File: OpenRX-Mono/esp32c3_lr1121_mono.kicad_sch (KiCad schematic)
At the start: 45 parts, among them T1 0900PC16J0042001E, U1 ESP32-C3FH4, U2 TLV75533PDQNR, U3 RFX2401C, U4 LR1121IMLTRT, U5 OW2EL89CENUXFMYLC-32M, X1 CJ17-400001010B20

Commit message: Add LCSC C430052 for 24nH XTAL_P inductor on Mono
Mono L2 (24nH 0201) was missing LCSC field.
Lite still needs 24nH inductor added in KiCad GUI.
Gemini is parked — still a Mono copy, not yet dual-radio.
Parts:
- added L2: 24nH, Inductor_SMD:L_0201_0603Metric, symbol Device:L
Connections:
- net XTAL_P: now also L2.2; no longer C6.1, X1.1
- new net: C6.1, L2.1, X1.1
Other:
- moved on the sheet: AE1, C1, C10, C11, C12, C13, C19, C2, C20, C21, C22, C23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

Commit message: OpenRX-Gemini: dual LR1121 schematic complete, 0 ERC errors
- Radio 1 (U4): sub-GHz via Johanson IPD → JP1 UFL
- Radio 2 (U9): 2.4GHz via RFX2401C (U10) → DEA (USB2) → JP3 UFL
- Shared SPI bus (SCK/MISO/MOSI), separate NSS/IRQ/BUSY/RST per radio
- Radio 2 control: GPIO10=NSS2, GPIO9=IRQ2, GPIO1=BUSY2, GPIO0=RST2
- FEM driven by Radio 2 RFSW (DIO5→RXEN, DIO6→TXEN)
- Radio 1 DIO5/DIO6 have 100k pull-downs (disconnected from FEM)
- No LED (GPIO10 used for NSS2), no boot button (GPIO9 used for IRQ2)
- Still needs: 10k pull-up on NSS2
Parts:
- L2: LCSC C430052 -> C206441
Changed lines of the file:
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@@
 			)
 		)
-		(property "LCSC" ""
+		(property "LCSC" "C206441"
 			(at -246.38 2.54 0)
 			(hide yes)
@@
 			(effects
 				(font
-					(size 1.27 1.27)
-				)
-			)
-		)
-		(property "LCSC" "C430052"
-			(at 0 0 0)
-			(show_name no)
-			(do_not_autoplace no)
-			(hide yes)
-			(effects
-				(font

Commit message: Swap all solder pads to 1.2x2.0mm rounded (25%) across Lite, Mono, Gemini
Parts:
- TP1, TP2, TP3, TP4: footprint OpenRX-Shared:SolderPad_1.0x1.5mm -> OpenRX-Shared:SolderPad_1.2x2.0mm
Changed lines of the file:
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@@
 			)
 		)
-		(property "Footprint" "OpenRX-Shared:SolderPad_1.0x1.5mm"
+		(property "Footprint" "OpenRX-Shared:SolderPad_1.2x2.0mm"
 			(at 152.4 116.84 0)
 			(hide yes)
@@
 			)
 		)
-		(property "Footprint" "OpenRX-Shared:SolderPad_1.0x1.5mm"
+		(property "Footprint" "OpenRX-Shared:SolderPad_1.2x2.0mm"
 			(at 82.55 72.39 0)
 			(hide yes)
@@
 			)
 		)
-		(property "Footprint" "OpenRX-Shared:SolderPad_1.0x1.5mm"
+		(property "Footprint" "OpenRX-Shared:SolderPad_1.2x2.0mm"
 			(at 82.55 74.93 0)
 			(hide yes)
@@
 			)
 		)
-		(property "Footprint" "OpenRX-Shared:SolderPad_1.0x1.5mm"
+		(property "Footprint" "OpenRX-Shared:SolderPad_1.2x2.0mm"
 			(at 152.4 106.68 0)
 			(hide yes)

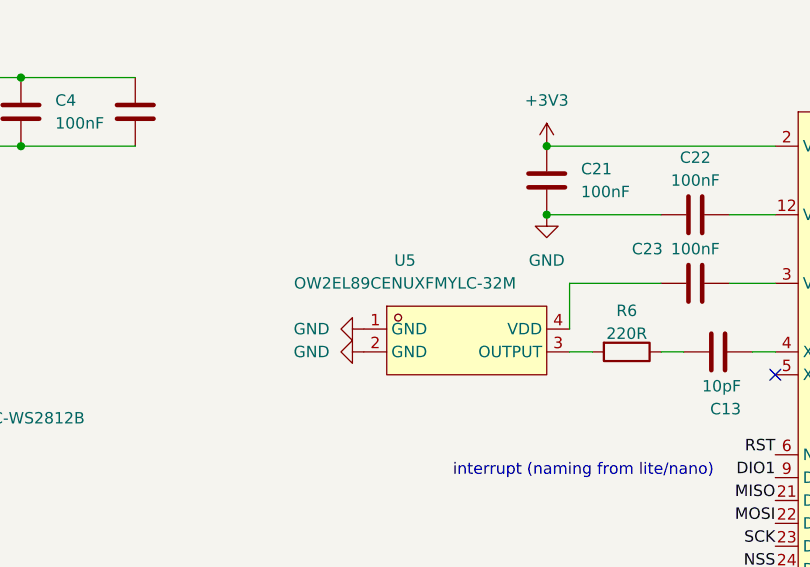
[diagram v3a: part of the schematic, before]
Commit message: Swap 32MHz TCXO to smaller 2016 package (C22381772)
OW2EL89 (3225, 3.2x2.5mm) → OW7EL89 (2016, 2.0x1.6mm)
Same YXC family, same pinout, same specs. Saves 1.2x0.9mm per TCXO.
Affects Mono (1x) and Gemini (2x).
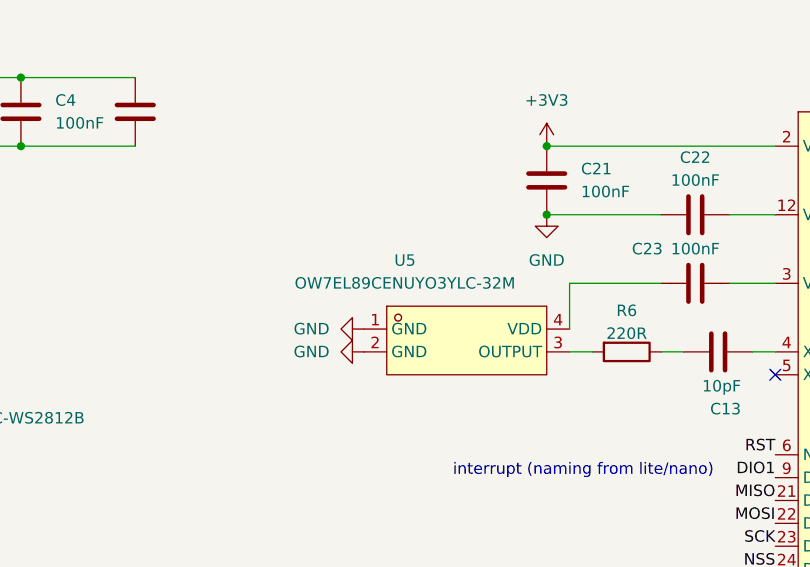
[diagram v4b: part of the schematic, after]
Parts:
- U5: value OW2EL89CENUXFMYLC-32M -> OW7EL89CENUYO3YLC-32M; footprint OpenRX-Shared:OSC-SMD_4P-L3.2-W2.5-BL -> OpenRX-Shared:OSC-SMD_4P-L2.0-W1.6-BL_TXC_7Z; symbol OpenRX-Shared:OW2EL89CENUXFMYLC-32M -> OpenRX-Shared:OW7EL89CENUYO3YLC-32M; LCSC C22434888 -> C22381772; LCSC Part C22434888 -> C22381772
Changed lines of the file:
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@@
 	)
 	(symbol
-		(lib_id "OpenRX-Shared:OW2EL89CENUXFMYLC-32M")
+		(lib_id "OpenRX-Shared:OW7EL89CENUYO3YLC-32M")
 		(at 217.17 58.42 0)
 		(unit 1)
@@
 			)
 		)
-		(property "Value" "OW2EL89CENUXFMYLC-32M"
+		(property "Value" "OW7EL89CENUYO3YLC-32M"
 			(at 210.312 52.07 0)
 			(show_name no)
@@
 			)
 		)
-		(property "Footprint" "OpenRX-Shared:OSC-SMD_4P-L3.2-W2.5-BL"
+		(property "Footprint" "OpenRX-Shared:OSC-SMD_4P-L2.0-W1.6-BL_TXC_7Z"
 			(at 217.17 67.31 0)
 			(hide yes)
@@
 			)
 		)
-		(property "LCSC Part" "C22434888"
+		(property "LCSC Part" "C22381772"
 			(at 217.17 69.85 0)
 			(hide yes)
@@
 			)
 		)
-		(property "LCSC" "C22434888"
+		(property "LCSC" "C22381772"
 			(at -15.24 0 0)
 			(hide yes)

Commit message: FINAL_NETLIST v3: SKY13588 as band combiner, RFX2401C kept for 100mW
Based on RadioMaster XR4 teardown analysis:
- SKY13588 serves as both sub-GHz path switch AND band combiner
- Johanson IPD in direct-tie mode (RX/TX_LP/TX_HP joined) → SKY13588 J1
- 2.4GHz: RFIO_HF → DEA LPF → RFX2401C → SKY13588 J2
- SKY13588 RFC → DC block → UFL → dual-band antenna
- RFX2401C kept for 100mW market parity
- Button imported (C2976675, 3x2mm SMD)
- RFSW truth table: DIO7/DIO8 control band, DIO5/DIO6 control RFX2401C
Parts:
- removed C26: 1uF, Capacitor_SMD:C_0201_0603Metric, symbol Device:C
- removed JP2: U.FL-R-SMT-1(80), OpenRX-Shared:RF-SMD_FRF05002-JSS103M, symbol OpenRX-Shared:U.FL-R-SMT-1(80)
- removed U3: RFX2401C, OpenRX-Shared:QFN-16_L3.0-W3.0-P0.50-BL-EP1.7, symbol OpenRX-Shared:RFX2401C
- removed USB1: DEA102700LT-6307A2, OpenRX-Shared:FILTER-SMD_4P-L1.0-W0.5-L_DEA102700LT-XXX, symbol OpenRX-Shared:DEA102700LT-6307A2
- added U3: TS2306A 240GF MSM 9_C2976675, OpenRX-Shared:SW-SMD_4P-L3.0-W2.0-P0.85-LS3.5, symbol OpenRX-Shared:TS2306A240GFMSM9_C2976675
- added U6: SKY13588-460LF, OpenRX-Shared:QFN-12_L2.0-W2.0-P0.50-BL-EP0.8, symbol OpenRX-Shared:SKY13588-460LF
- added USB2: DEA102700LT-6307A2, OpenRX-Shared:FILTER-SMD_4P-L1.0-W0.5-L_DEA102700LT-XXX, symbol OpenRX-Shared:DEA102700LT-6307A2
- C25: value 220pF -> 100nF; LCSC C62548 -> C76939
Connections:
- net RXEN is gone; now on an unnamed net: U4.20 (DIO5)
- net TXEN is gone; now on an unnamed net: U4.19 (DIO6)
- net +3V3: now also U6.6 (VDD)
- net GND: now also C23.1, U3.2, U6.10 (GND), U6.12 (GND), U6.13 (EP), U6.2 (GND), U6.7 (GND), U6.8 (GND), USB2.2 (GND), USB2.4 (GND)
- net LED: now also U1.14 (GPIO8); no longer U1.16 (GPIO10)
- net MISO: now also U1.10 (MTDI); no longer U1.12 (MTCK)
- net MOSI: now also U1.9 (MTMS); no longer U1.13 (MTDO)
- net SCK: now also U1.12 (MTCK); no longer U1.9 (MTMS)
- net IRQ1: now reaches U1.5 (XTAL_32K_N)
- net IRQ1: now also U4.9 (DIO9)
- net at U5.4 (VDD): now also C23.2, U4.3 (VTCXO); no longer C23.1
- net at R5.2: no longer U4.10 (DIO8)
- net at R7.2: no longer U4.11 (DIO7)
- net at U4.26 (RFIO_HF): now also USB2.1 (IN)
- net BUSY renamed BUSY1
- net CHIP_BOOT renamed BUTTON
- net BUTTON: now also U3.1
- removed net DIO1: U1.10 (MTDI), U4.9 (DIO9)
- net NSS renamed NSS1
- net NSS1: now also U1.13 (MTDO); no longer U1.14 (GPIO8)
- net RST renamed RST1
- new net: JP1.1 (SIG), U6.11 (RFC), USB2.3 (OUT)
- new net: T1.6 (RX), U6.1 (J1)
- new net: T1.8 (TX_LP), U6.9 (J2)
- new net: T1.9 (TX_HP), U6.3 (J3)
- new net DIO7-1: U4.11 (DIO7), U6.4 (V1)
- new net DIO8-1: U4.10 (DIO8), U6.5 (V2)
- no-connect marks 21 -> 19
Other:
- note removed: "interrupt (naming from lite/nano)"
- moved on the sheet: C23, JP1, R2, T1

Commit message: Mono schematic v4: complete RF chain verified
Verified netlist:
- LR1121 → IPD (direct-tie, pins 6+8+9 joined) → SKY13588 J1 ✓
- LR1121 RFIO_HF → DEA LPF → RFX2401C TXRX ✓
- RFX2401C ANT → 0.3pF shunt → SKY13588 J2 ✓
- SKY13588 RFC → UFL ✓
- DIO7→V1, DIO8→V2 (band select) ✓
- DIO5→RXEN, DIO6→TXEN (RFX2401C control) ✓
- GPIO map matches Generic C3 LR1121 target ✓
- Added LCSC to 220pF, RFX2401C, button
- 1 ERC error: GPIO10 needs NC marker
- 0.3pF has no LCSC (layout pad for tuning)
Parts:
- removed R5, R7: 100k, Resistor_SMD:R_0201_0603Metric, symbol Device:R
- added C14: 1uF, Capacitor_SMD:C_0201_0603Metric, symbol Device:C
- added C15: 220pF, Capacitor_SMD:C_0201_0603Metric, symbol Device:C
- added C16: 0.3pF, Capacitor_SMD:C_0201_0603Metric, symbol Device:C
- added U7: RFX2401C, OpenRX-Shared:QFN-16_L3.0-W3.0-P0.50-BL-EP1.7, symbol OpenRX-Shared:RFX2401C
- U3: LCSC (none) -> C2976675
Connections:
- net +3V3: now also C14.1, C15.1, U7.14 (VDD), U7.16 (VDD)
- net GND: now also C14.2, C15.2, C16.2, U7.1 (GND), U7.11 (GND), U7.12 (GND), U7.15 (GND), U7.17 (EP), U7.2 (GND), U7.3 (GND), U7.7 (GND), U7.8 (GND), U7.9 (GND)
- net at JP1.1 (SIG), U6.11 (RFC): no longer USB2.3 (OUT)
- net TXEN: now reaches U4.19 (DIO6)
- net TXEN: now also U7.5 (TXEN)
- net RXEN: now reaches U4.20 (DIO5)
- net RXEN: now also U7.6 (RXEN)
- net at T1.6 (RX), U6.1 (J1): now also T1.8 (TX_LP), T1.9 (TX_HP)
- net at U6.9 (J2): now also C16.1, U7.10 (ANT); no longer T1.8 (TX_LP)
- net at U6.3 (J3): no longer T1.9 (TX_HP)
- new net: U7.4 (TXRX), USB2.3 (OUT)
- no-connect marks 19 -> 21
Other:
- moved on the sheet: C13, C20, C21, C22, C23, C24, C25, JP1, L1, R6, T1, U4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

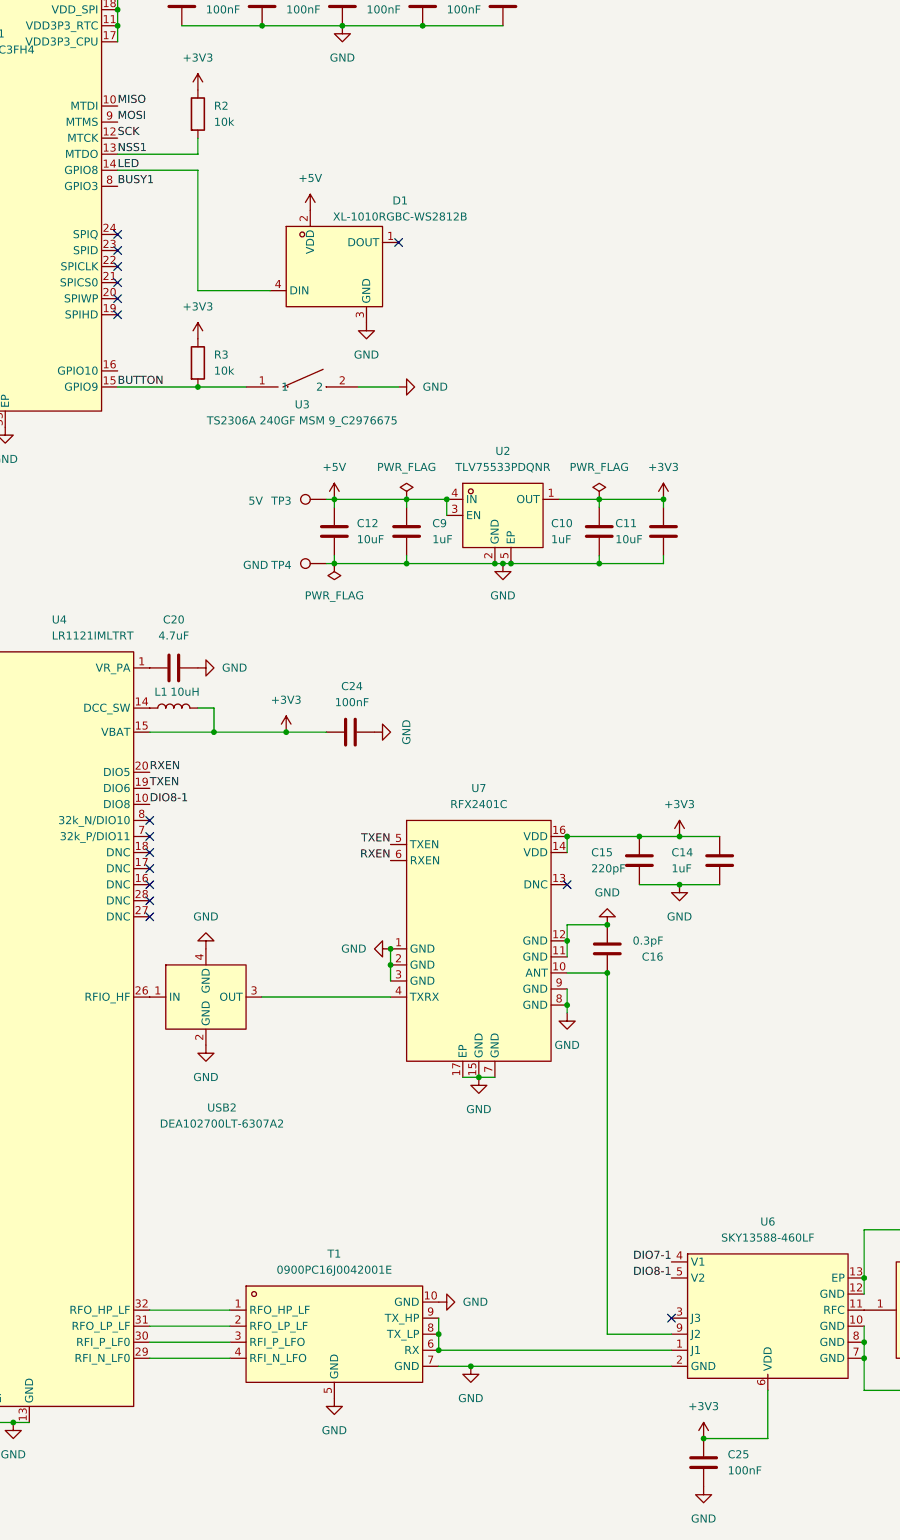
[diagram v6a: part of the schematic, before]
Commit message: Gemini: copy Mono schematic as base for dual-radio build
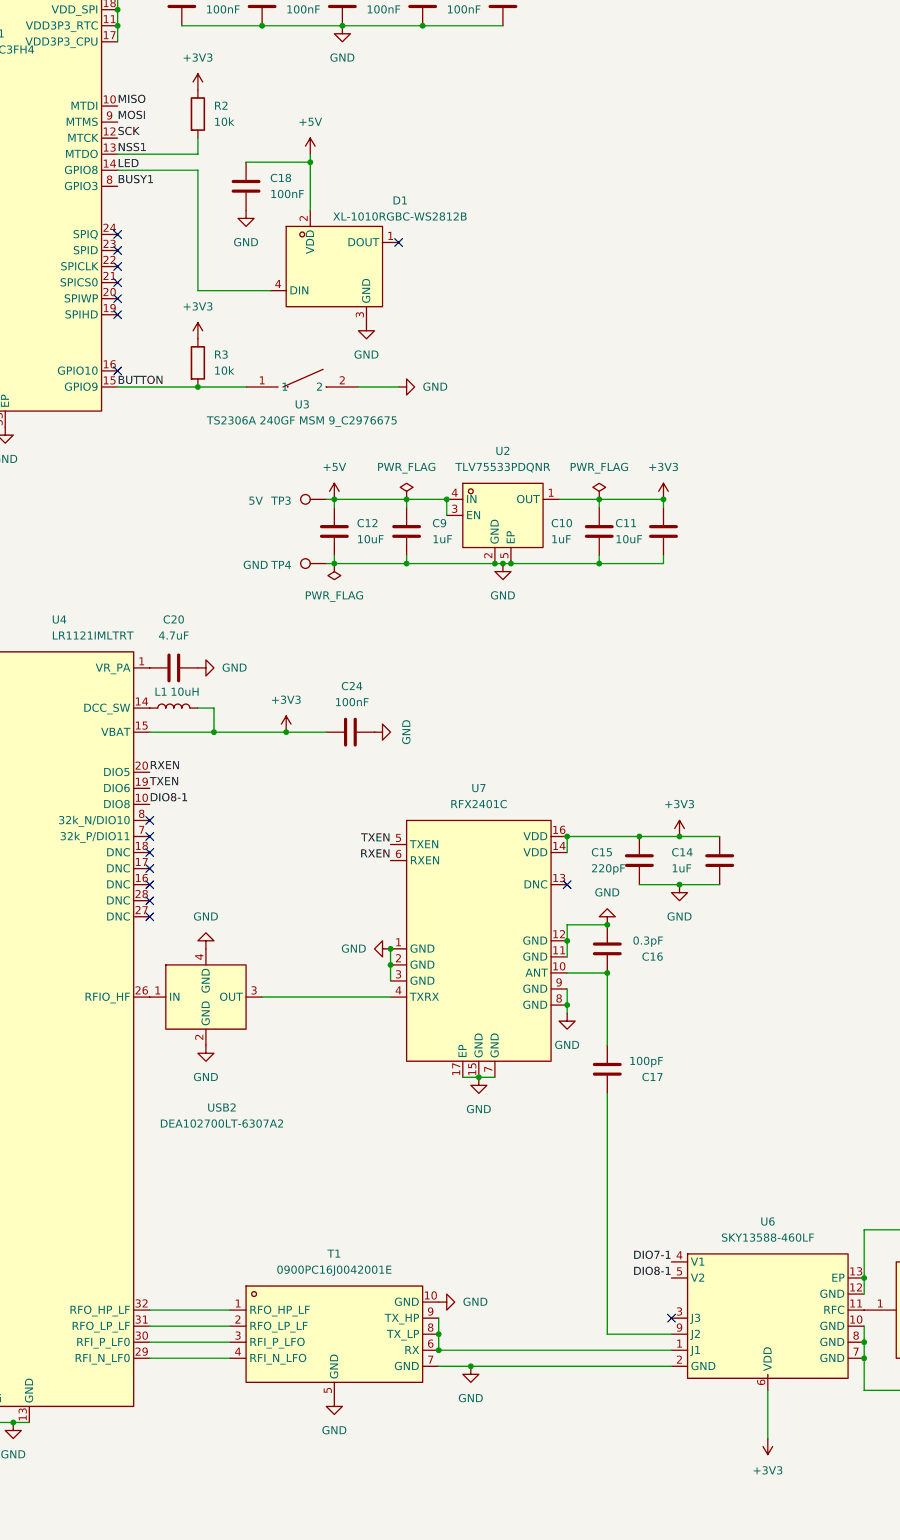
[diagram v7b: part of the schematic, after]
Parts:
- removed C25: 100nF, Capacitor_SMD:C_0201_0603Metric, symbol Device:C
- added C17: 100pF, Capacitor_SMD:C_0201_0603Metric, symbol Device:C
- added C18: 100nF, Capacitor_SMD:C_0201_0603Metric, symbol Device:C
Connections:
- net +5V: now also C18.1
- net GND: now also C18.2
- net at C16.1, U7.10 (ANT): now also C17.2; no longer U6.9 (J2)
- new net: C17.1, U6.9 (J2)
- no-connect marks 21 -> 22
